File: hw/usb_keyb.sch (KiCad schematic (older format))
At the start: 103 parts, among them J1 POWER, J10 SPI, J11 ZX BUS, J12 ID, J13 ID, J2 Micro_SD_Card, J3 USB_1, J4 USB_2, J5 MX_ROW, J6 MX_COL, J7 I2C, J8 UART, J9 PROG, SW1 RESET, U1 LM3671MF, U2 STM32F407VETx, U3 STMPS2141STR, U4 STMPS2141STR, U5 74ALVC164245, U6 74ALVC164245, U7 74ALVC164245, Y1 8MHz

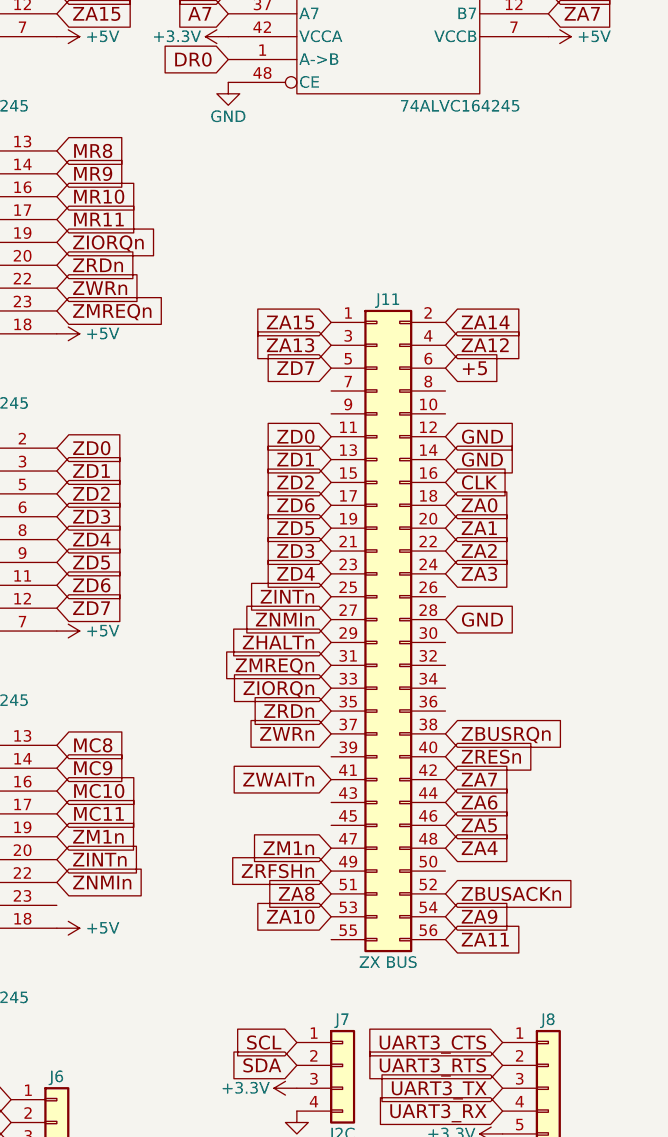
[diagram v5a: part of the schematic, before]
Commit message: Изменён разъём ZX-BUS, обновлена компоновка
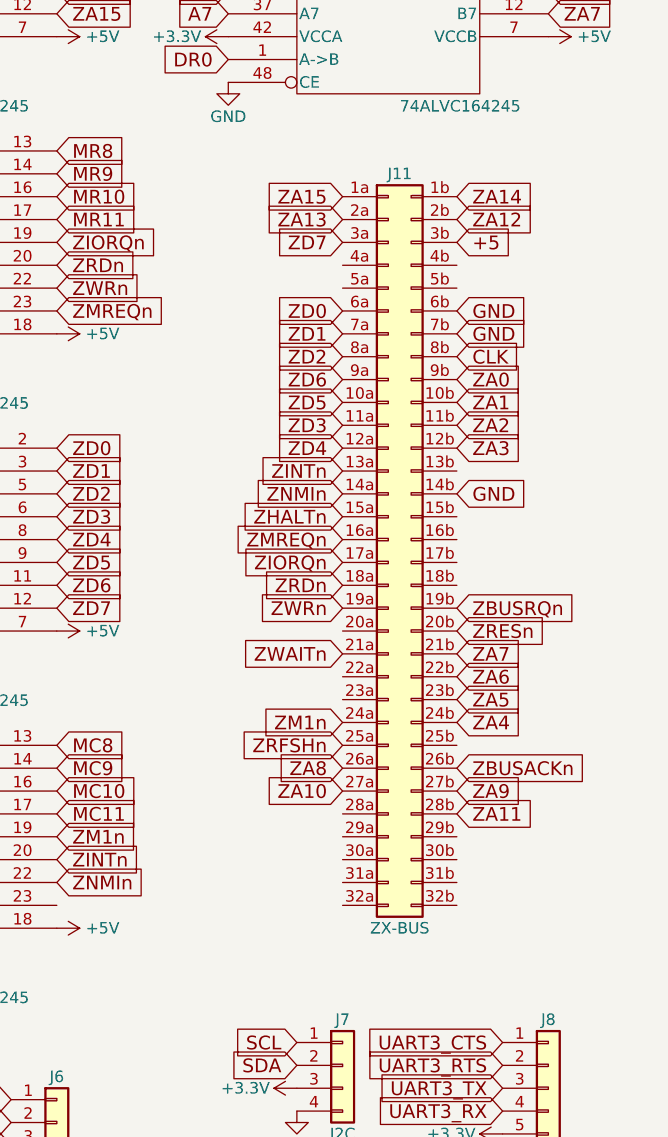
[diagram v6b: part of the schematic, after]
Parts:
- removed J11: ZX BUS, symbol Conn_02x28_Odd_Even
- added J11: ZX-BUS, Connectors_IEC_DIN:Socket_DIN41612-CaseC1-AC-Female-64Pin-2rows, symbol Conn_02x32_Row_Letter_Last
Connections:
- net +5: now also J11.3b (Pin_3b)
- net CLK: now also J11.8b (Pin_8b)
- net GND: now also J11.14b (Pin_14b), J11.6b (Pin_6b), J11.7b (Pin_7b)
- net ZA0: now also J11.9b (Pin_9b)
- net ZA1: now also J11.10b (Pin_10b)
- net ZA10: now also J11.27a (Pin_27a)
- net ZA11: now also J11.28b (Pin_28b)
- net ZA12: now also J11.2b (Pin_2b)
- net ZA13: now also J11.2a (Pin_2a)
- net ZA14: now also J11.1b (Pin_1b)
- net ZA15: now also J11.1a (Pin_1a)
- net ZA2: now also J11.11b (Pin_11b)
- net ZA3: now also J11.12b (Pin_12b)
- net ZA4: now also J11.24b (Pin_24b)
- net ZA5: now also J11.23b (Pin_23b)
- net ZA6: now also J11.22b (Pin_22b)
- net ZA7: now also J11.21b (Pin_21b)
- net ZA8: now also J11.26a (Pin_26a)
- net ZA9: now also J11.27b (Pin_27b)
- net ZBUSACKn: now also J11.26b (Pin_26b)
- net ZBUSRQn: now also J11.19b (Pin_19b)
- net ZD0: now also J11.6a (Pin_6a)
- net ZD1: now also J11.7a (Pin_7a)
- net ZD2: now also J11.8a (Pin_8a)
- net ZD3: now also J11.11a (Pin_11a)
- net ZD4: now also J11.12a (Pin_12a)
- net ZD5: now also J11.10a (Pin_10a)
- net ZD6: now also J11.9a (Pin_9a)
- net ZD7: now also J11.3a (Pin_3a)
- net ZHALTn: now also J11.15a (Pin_15a)
- net ZINTn: now also J11.13a (Pin_13a)
- net ZIORQn: now also J11.17a (Pin_17a)
- net ZM1n: now also J11.24a (Pin_24a)
- net ZMREQn: now also J11.16a (Pin_16a)
- net ZNMIn: now also J11.14a (Pin_14a)
- net ZRDn: now also J11.18a (Pin_18a)
- net ZRESn: now also J11.20b (Pin_20b)
- net ZRFSHn: now also J11.25a (Pin_25a)
- net ZWAITn: now also J11.21a (Pin_21a)
- net ZWRn: now also J11.19a (Pin_19a)
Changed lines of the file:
@@
 Text GLabel 10750 6550 2    60   Input ~ 0
 HS_ID
-Text GLabel 14450 5150 0    60   Input ~ 0
+Text GLabel 14500 4600 0    60   Input ~ 0
 ZA15
-Text GLabel 14950 5150 2    60   Input ~ 0
+Text GLabel 15000 4600 2    60   Input ~ 0
 ZA14
-Text GLabel 14450 5250 0    60   Input ~ 0
+Text GLabel 14500 4700 0    60   Input ~ 0
 ZA13
-Text GLabel 14950 5250 2    60   Input ~ 0
+Text GLabel 15000 4700 2    60   Input ~ 0
 ZA12
-Text GLabel 14450 5350 0    60   Input ~ 0
+Text GLabel 14500 4800 0    60   Input ~ 0
 ZD7
-Text GLabel 14950 5350 2    60   Input ~ 0
+Text GLabel 15000 4800 2    60   Input ~ 0
 +5
-Text GLabel 14450 5650 0    60   Input ~ 0
+Text GLabel 14500 5100 0    60   Input ~ 0
 ZD0
-Text GLabel 14450 5750 0    60   Input ~ 0
+Text GLabel 14500 5200 0    60   Input ~ 0
 ZD1
-Text GLabel 14450 5850 0    60   Input ~ 0
+Text GLabel 14500 5300 0    60   Input ~ 0
 ZD2
-Text GLabel 14450 5950 0    60   Input ~ 0
+Text GLabel 14500 5400 0    60   Input ~ 0
 ZD6
-Text GLabel 14450 6050 0    60   Input ~ 0
+Text GLabel 14500 5500 0    60   Input ~ 0
 ZD5
-Text GLabel 14450 6150 0    60   Input ~ 0
+Text GLabel 14500 5600 0    60   Input ~ 0
 ZD3
-Text GLabel 14450 6250 0    60   Input ~ 0
+Text GLabel 14500 5700 0    60   Input ~ 0
 ZD4
-Text GLabel 14450 6350 0    60   Input ~ 0
+Text GLabel 14500 5800 0    60   Input ~ 0
 ZINTn
-Text GLabel 14450 6450 0    60   Input ~ 0
+Text GLabel 14500 5900 0    60   Input ~ 0
 ZNMIn
-Text GLabel 14450 6550 0    60   Input ~ 0
+Text GLabel 14500 6000 0    60   Input ~ 0
 ZHALTn
-Text GLabel 14450 6650 0    60   Input ~ 0
+Text GLabel 14500 6100 0    60   Input ~ 0
 ZMREQn
-Text GLabel 14450 6750 0    60   Input ~ 0
+Text GLabel 14500 6200 0    60   Input ~ 0
 ZIORQn
-Text GLabel 14450 6850 0    60   Input ~ 0
+Text GLabel 14500 6300 0    60   Input ~ 0
 ZRDn
-Text GLabel 14450 6950 0    60   Input ~ 0
+Text GLabel 14500 6400 0    60   Input ~ 0
 ZWRn
-Text GLabel 14450 7150 0    60   Input ~ 0
+Text GLabel 14500 6600 0    60   Input ~ 0
 ZWAITn
-Text GLabel 14450 7450 0    60   Input ~ 0
+Text GLabel 14500 6900 0    60   Input ~ 0
 ZM1n
-Text GLabel 14450 7550 0    60   Input ~ 0
+Text GLabel 14500 7000 0    60   Input ~ 0
 ZRFSHn
-Text GLabel 14450 7650 0    60   Input ~ 0
+Text GLabel 14500 7100 0    60   Input ~ 0
 ZA8
-Text GLabel 14450 7750 0    60   Input ~ 0
+Text GLabel 14500 7200 0    60   Input ~ 0
 ZA10
-Text GLabel 14950 5650 2    60   Input ~ 0
+Text GLabel 15000 5100 2    60   Input ~ 0
 GND
-Text GLabel 14950 5750 2    60   Input ~ 0
+Text GLabel 15000 5200 2    60   Input ~ 0
 GND
-Text GLabel 14950 5850 2    60   Input ~ 0
+Text GLabel 15000 5300 2    60   Input ~ 0
 CLK
-Text GLabel 14950 5950 2    60   Input ~ 0
+Text GLabel 15000 5400 2    60   Input ~ 0
 ZA0
-Text GLabel 14950 6050 2    60   Input ~ 0
+Text GLabel 15000 5500 2    60   Input ~ 0
 ZA1
-Text GLabel 14950 6150 2    60   Input ~ 0
+Text GLabel 15000 5600 2    60   Input ~ 0
 ZA2
-Text GLabel 14950 6250 2    60   Input ~ 0
+Text GLabel 15000 5700 2    60   Input ~ 0
 ZA3
-Text GLabel 14950 6450 2    60   Input ~ 0
+Text GLabel 15000 5900 2    60   Input ~ 0
 GND
-Text GLabel 14950 6950 2    60   Input ~ 0
+Text GLabel 15000 6400 2    60   Input ~ 0
 ZBUSRQn
-Text GLabel 14950 7050 2    60   Input ~ 0
+Text GLabel 15000 6500 2    60   Input ~ 0
 ZRESn
-Text GLabel 14950 7150 2    60   Input ~ 0
+Text GLabel 15000 6600 2    60   Input ~ 0
 ZA7
-Text GLabel 14950 7250 2    60   Input ~ 0
+Text GLabel 15000 6700 2    60   Input ~ 0
 ZA6
-Text GLabel 14950 7350 2    60   Input ~ 0
+Text GLabel 15000 6800 2    60   Input ~ 0
 ZA5
-Text GLabel 14950 7450 2    60   Input ~ 0
+Text GLabel 15000 6900 2    60   Input ~ 0
 ZA4
-Text GLabel 14950 7650 2    60   Input ~ 0
+Text GLabel 15000 7100 2    60   Input ~ 0
 ZBUSACKn
-Text GLabel 14950 7750 2    60   Input ~ 0
+Text GLabel 15000 7200 2    60   Input ~ 0
 ZA9
-Text GLabel 14950 7850 2    60   Input ~ 0
+Text GLabel 15000 7300 2    60   Input ~ 0
 ZA11
-$Comp
-L Conn_02x28_Odd_Even J11
-U 1 1 5AB3CEB4
-P 14650 6450
-F 0 "J11" H 14700 7850 50  0000 C CNN
-F 1 "ZX BUS" H 14700 4950 50  0000 C CNN
-F 2 "" H 14650 6450 50  0001 C CNN
-F 3 "" H 14650 6450 50  0001 C CNN
-	1    14650 6450
-	1    0    0    -1
-$EndComp
 Text GLabel 13250 5700 2    60   Input ~ 0
 ZD0
@@
 Wire Wire Line
 	7650 2400 7650 2150
+$Comp
+L Conn_02x32_Row_Letter_Last J11
+U 1 1 5ABDA855
+P 14700 6100
+F 0 "J11" H 14750 7700 50  0000 C CNN
+F 1 "ZX-BUS" H 14750 4400 50  0000 C CNN
+F 2 "Connectors_IEC_DIN:Socket_DIN41612-CaseC1-AC-Female-64Pin-2rows" H 14700 6100 50  0001 C CNN
+F 3 "" H 14700 6100 50  0001 C CNN
+	1    14700 6100
+	1    0    0    -1
+$EndComp
 $EndSCHEMATC

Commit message: Убраны буферные элементы, все внешние сигналы будут Open Drain
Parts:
- removed C19, C20, C21, C22, C23, C24, C25, C26, C27, C28, C29, C30: 100n, Capacitors_SMD:C_0805, symbol C
- removed U5, U6, U7: 74ALVC164245, Housings_SSOP:SSOP-48_7.5x15.9mm_Pitch0.635mm, symbol 74ALVC164245
- added R48, R49, R50, R51, R52, R53, R54, R55, R56, R57, R58: 10k, Resistors_SMD:R_0805, symbol R
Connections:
- net A0 is gone; now on net ZA0: U2.84 (PD3/FSMC_CLK/USART2_CTS)
- net A1 is gone; now on net ZA1: U2.85 (PD4/FSMC_NOE/USART2_RTS)
- net A2 is gone; now on net ZA2: U2.86 (PD5/FSMC_NWE/USART2_TX)
- net A3 is gone; now on net ZA3: U2.87 (PD6/FSMC_NWAIT/USART2_RX)
- net A4 is gone; now on net ZA4: U2.88 (PD7/FSMC_NCE2/FSMC_NE1/USART2_CK)
- net A5 is gone; now on net ZA5: U2.55 (PD8/FSMC_D13/FSMC_DA13/USART3_TX)
- net A6 is gone; now on net ZA6: U2.56 (PD9/DAC_EXTI9/FSMC_D14/FSMC_DA14/USART3_RX)
- net A7 is gone; now on net ZA7: U2.57 (PD10/FSMC_D15/FSMC_DA15/USART3_CK)
- net C0 is gone; now on net ZD0: R36.2
- net C1 is gone; now on net ZD1: R37.2
- net C10 is gone; now on net MC10: R46.2
- net C11 is gone; now on net MC11: R47.2
- net C2 is gone; now on net ZD2: R38.2
- net C3 is gone; now on net ZD3: R39.2
- net C4 is gone; now on net ZD4: R40.2
- net C5 is gone; now on net ZD5: R41.2
- net C6 is gone; now on net ZD6: R42.2
- net C7 is gone; now on net ZD7: R43.2
- net C8 is gone; now on net MC8: R44.2
- net C9 is gone; now on net MC9: R45.2
- net I0 is gone; now on net ZA8: U2.15 (ADC1_IN10/ADC2_IN10/ADC3_IN10/USB_OTG_HS_ULPI_STP/PC0)
- net I1 is gone; now on net ZA9: U2.16 (ADC1_IN11/ADC2_IN11/ADC3_IN11/ETH_MDC/PC1)
- net I10 is gone; now on net MR10: U2.60 (PD13/FSMC_A18/TIM4_CH2)
- net I11 is gone; now on net MR11: U2.61 (PD14/FSMC_D0/FSMC_DA0/TIM4_CH3)
- net I2 is gone; now on net ZA10: U2.17 (ADC1_IN12/ADC2_IN12/ADC3_IN12/ETH_TXD2/I2S2_ext_SD/SPI2_MISO/USB_OTG_HS_ULPI_DIR/PC2)
- net I3 is gone; now on net ZA11: U2.18 (ADC1_IN13/ADC2_IN13/ADC3_IN13/ETH_TX_CLK/I2S2_SD/SPI2_MOSI/USB_OTG_HS_ULPI_NXT/PC3)
- net I4 is gone; now on net ZA12: U2.33 (ADC1_IN14/ADC2_IN14/ETH_RXD0/PC4)
- net I5 is gone; now on net ZA13: U2.34 (ADC1_IN15/ADC2_IN15/ETH_RXD1/PC5)
- net I6 is gone; now on net ZA14: U2.63 (DCMI_D0/I2S2_MCK/SDIO_D6/TIM3_CH1/TIM8_CH1/USART6_TX/PC6)
- net I7 is gone; now on net ZA15: U2.64 (DCMI_D1/I2S3_MCK/SDIO_D7/TIM3_CH2/TIM8_CH2/USART6_RX/PC7)
- net I8 is gone; now on net MR8: U2.81 (PD0/CAN1_RX/FSMC_D2/FSMC_DA2)
- net I9 is gone; now on net MR9: U2.82 (PD1/CAN1_TX/FSMC_D3/FSMC_DA3)
- net INT0 is gone; now on net ZIORQn: R20.2, U2.23 (ADC1_IN0/ADC2_IN0/ADC3_IN0/ETH_CRS/SYS_WKUP/TIM2_CH1/TIM2_ETR/TIM5_CH1/TIM8_ETR/UART4_TX/USART2_CTS/PA0)
- net INT1 is gone; now on net ZRDn: R21.2, U2.24 (ADC1_IN1/ADC2_IN1/ADC3_IN1/ETH_REF_CLK/ETH_RX_CLK/TIM2_CH2/TIM5_CH2/UART4_RX/USART2_RTS/PA1)
- net INT2 is gone; now on net ZWRn: R22.2, U2.25 (ADC1_IN2/ADC2_IN2/ADC3_IN2/ETH_MDIO/TIM2_CH3/TIM5_CH3/TIM9_CH1/USART2_TX/PA2)
- net INT3 is gone; now on net ZMREQn: R23.2, U2.26 (ADC1_IN3/ADC2_IN3/ADC3_IN3/ETH_COL/TIM2_CH4/TIM5_CH4/TIM9_CH2/USART2_RX/USB_OTG_HS_ULPI_D0/PA3)
- net INTn is gone; now on net ZINTn: U2.44 (PE13/FSMC_D10/FSMC_DA10/TIM1_CH3)
- net M1n is gone; now on net ZM1n: U2.43 (PE12/FSMC_D9/FSMC_DA9/TIM1_CH3N)
- net NMIn is gone; now on net ZNMIn: U2.45 (PE14/FSMC_D11/FSMC_DA11/TIM1_CH4)
- net O0 is gone; now on net ZD0: U2.97 (PE0/DCMI_D2/FSMC_NBL0/TIM4_ETR)
- net O1 is gone; now on net ZD1: U2.98 (PE1/DCMI_D3/FSMC_NBL1)
- net O10 is gone; now on net MC10: U2.41 (PE10/FSMC_D7/FSMC_DA7/TIM1_CH2N)
- net O11 is gone; now on net MC11: U2.42 (PE11/ADC1_EXTI11/ADC2_EXTI11/ADC3_EXTI11/FSMC_D8/FSMC_DA8/TIM1_CH2)
- net O2 is gone; now on net ZD2: U2.1 (PE2/ETH_TXD3/FSMC_A23/SYS_TRACECLK)
- net O3 is gone; now on net ZD3: U2.2 (PE3/FSMC_A19/SYS_TRACED0)
- net O4 is gone; now on net ZD4: U2.3 (PE4/DCMI_D4/FSMC_A20/SYS_TRACED1)
- net O5 is gone; now on net ZD5: U2.4 (PE5/DCMI_D6/FSMC_A21/SYS_TRACED2/TIM9_CH1)
- net O6 is gone; now on net ZD6: U2.5 (PE6/DCMI_D7/FSMC_A22/SYS_TRACED3/TIM9_CH2)
- net O7 is gone; now on net ZD7: U2.38 (PE7/FSMC_D4/FSMC_DA4/TIM1_ETR)
- net O8 is gone; now on net MC8: U2.39 (PE8/FSMC_D5/FSMC_DA5/TIM1_CH1N)
- net O9 is gone; now on net MC9: U2.40 (PE9/DAC_EXTI9/FSMC_D6/FSMC_DA6/TIM1_CH1)
- net R0 is gone; now on net ZA8: R24.2
- net R1 is gone; now on net ZA9: R25.2
- net R10 is gone; now on net MR10: R34.2
- net R11 is gone; now on net MR11: R35.2
- net R2 is gone; now on net ZA10: R26.2
- net R3 is gone; now on net ZA11: R27.2
- net R4 is gone; now on net ZA12: R28.2
- net R5 is gone; now on net ZA13: R29.2
- net R6 is gone; now on net ZA14: R30.2
- net R7 is gone; now on net ZA15: R31.2
- net R8 is gone; now on net MR8: R32.2
- net R9 is gone; now on net MR9: R33.2
- net +3V3: now also R48.1, R49.1, R50.1, R51.1, R52.1, R53.1, R54.1, R55.1, R56.1, R57.1, R58.1
- net ZA0: now also R51.2
- net ZA1: now also R52.2
- net ZA2: now also R53.2
- net ZA3: now also R54.2
- net ZA4: now also R55.2
- net ZA5: now also R56.2
- net ZA6: now also R57.2
- net ZA7: now also R58.2
- net ZINTn: now also R49.2
- net ZM1n: now also R48.2
- net ZNMIn: now also R50.2
- net DR0: no longer names the net of U2.35 (ADC1_IN8/ADC2_IN8/ETH_RXD2/TIM1_CH2N/TIM3_CH3/TIM8_CH2N/USB_OTG_HS_ULPI_D1/PB0)
- net DR1: no longer names the net of U2.36 (ADC1_IN9/ADC2_IN9/ETH_RXD3/TIM1_CH3N/TIM3_CH4/TIM8_CH3N/USB_OTG_HS_ULPI_D2/PB1)
- net DR2: no longer names the net of U2.37 (BOOT1/PB2)
- net DR3: no longer names the net of U2.89 (I2S3_CK/SPI1_SCK/SPI3_SCK/SYS_JTDO-SWO/TIM2_CH2/PB3)
- net DR4: no longer names the net of U2.90 (I2S3_ext_SD/SPI1_MISO/SPI3_MISO/SYS_JTRST/TIM3_CH1/PB4)
- net DR5: no longer names the net of U2.91 (CAN2_RX/DCMI_D10/ETH_PPS_OUT/I2C1_SMBA/I2S3_SD/SPI1_MOSI/SPI3_MOSI/TIM3_CH2/USB_OTG_HS_ULPI_D7/PB5)
- net DR6: no longer names the net of U2.95 (CAN1_RX/DCMI_D6/ETH_TXD3/I2C1_SCL/SDIO_D4/TIM10_CH1/TIM4_CH3/PB8)
- net DR7: no longer names the net of U2.96 (CAN1_TX/DAC_EXTI9/DCMI_D7/I2C1_SDA/I2S2_WS/SDIO_D5/SPI2_NSS/TIM11_CH1/TIM4_CH4/PB9)
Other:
- moved on the sheet: R20, R21, R22, R23

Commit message: Множественные изменения в схеме:
1) Заменён разъём USB на сдвоенный;
2) Добавлен Ethernet-PHY;
3) Изменено назначение служебных сигналов USB и интерфейсов;
4) внешние шины временно отключены от МК.
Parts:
- removed J12, J13: ID, Socket_Strips:Socket_Strip_Straight_1x01_Pitch2.54mm, symbol TEST_1P
- removed J4: USB_2, Connectors:USB_A, symbol USB_A
- added C19, C20, C21, C22, C24, C25, C26, C27, C29, C30, C31: 100n, Capacitors_SMD:C_0805, symbol C
- added C23, C28: 10u, Capacitors_Tantalum_SMD:CP_Tantalum_Case-A_EIA-3216-18_Reflow, symbol CP
- added J14: RJ45-TRANSFO, Projects:rj45_wurth-7499211122a, symbol RJ45-TRANSFO-RESCUE-usb_keyb
- added L2: 2.2µH, Inductors_SMD:L_0805, symbol L
- added R59, R60, R62, R63: 2k, Resistors_SMD:R_0805, symbol R
- added R61: 10k, Resistors_SMD:R_0805, symbol R
- added R64: 4k7, Resistors_SMD:R_0805, symbol R
- added R65: 150, Resistors_SMD:R_0805, symbol R
- added R66: 18, Resistors_SMD:R_0805, symbol R
- added R67, R68, R69, R70: 51, Resistors_SMD:R_0805, symbol R
- added R71, R72: 330, Resistors_SMD:R_0805, symbol R
- added U5: DP83848C, Housings_QFP:LQFP-48_7x7mm_Pitch0.5mm, symbol DP83848C
- added Y2: 50MHz, Crystals:Crystal_SMD_7050-4pin_7.0x5.0mm, symbol Crystal_GND24
- C17, C18: footprint Capacitors_Tantalum_SMD:CP_Tantalum_Case-A_EIA-3216-18_Hand -> Capacitors_Tantalum_SMD:CP_Tantalum_Case-A_EIA-3216-18_Reflow
- J2: symbol Micro_SD_Card -> Micro_SD_Card-RESCUE-usb_keyb
- J3: footprint Connectors:USB_A -> w_conn_pc:conn_usb_Ax2; symbol USB_A -> USB_A-RESCUE-usb_keyb
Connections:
- net +3V3: now also C19.1, C20.1, C21.1, C22.1, C23.1, C30.1, C31.1, J14.1 (TCT), J14.11 (LEDY_A), J14.13 (LEDG_A), L2.1, R59.1, R60.1, R61.1, R62.2, R63.2, R69.1, R70.1, U5.32 (IOVDD33), U5.48 (IOVDD33), Y2.4
- net CD: now also U2.64 (DCMI_D1/I2S3_MCK/SDIO_D7/TIM3_CH2/TIM8_CH2/USART6_RX/PC7); no longer U2.7 (ANTI_TAMP/RTC_AF1/PC13)
- net FS_PWR: now also U2.67 (I2C3_SCL/RCC_MCO_1/TIM1_CH1/USART1_CK/USB_OTG_FS_SOF/PA8); no longer U2.8 (RCC_OSC32_IN/PC14)
- net GND: now also J3.8 (GND), J3.9 (Shield), C19.2, C20.2, C21.2, C22.2, C23.2, C24.2, C25.2, C26.2, C27.2, C28.2, C29.2, C30.2, C31.2, J14.10, J14.15 (SHIELD), R66.1, U5.15 (AGND), U5.19 (AGND), U5.35 (IOGND), U5.36 (DGND), U5.47 (IOGND), Y2.2; no longer J3.5 (Shield)
- net HS_PWR: now also U2.63 (DCMI_D0/I2S2_MCK/SDIO_D6/TIM3_CH1/TIM8_CH1/USART6_TX/PC6); no longer U2.9 (ADC1_EXTI15/ADC2_EXTI15/ADC3_EXTI15/RCC_OSC32_OUT/PC15)
- net MC10: no longer U2.41 (PE10/FSMC_D7/FSMC_DA7/TIM1_CH2N)
- net MC11: no longer U2.42 (PE11/ADC1_EXTI11/ADC2_EXTI11/ADC3_EXTI11/FSMC_D8/FSMC_DA8/TIM1_CH2)
- net MC8: no longer U2.39 (PE8/FSMC_D5/FSMC_DA5/TIM1_CH1N)
- net MC9: no longer U2.40 (PE9/DAC_EXTI9/FSMC_D6/FSMC_DA6/TIM1_CH1)
- net MR10: no longer U2.60 (PD13/FSMC_A18/TIM4_CH2)
- net MR11: no longer U2.61 (PD14/FSMC_D0/FSMC_DA0/TIM4_CH3)
- net MR8: no longer U2.81 (PD0/CAN1_RX/FSMC_D2/FSMC_DA2)
- net MR9: no longer U2.82 (PD1/CAN1_TX/FSMC_D3/FSMC_DA3)
- net PA8: no longer U2.67 (I2C3_SCL/RCC_MCO_1/TIM1_CH1/USART1_CK/USB_OTG_FS_SOF/PA8)
- net SCL: no longer U2.92 (CAN2_TX/DCMI_D5/I2C1_SCL/TIM4_CH1/USART1_TX/PB6)
- net SDA: no longer U2.93 (DCMI_VSYNC/FSMC_NL/I2C1_SDA/TIM4_CH2/USART1_RX/PB7)
- net SPI_MISO: no longer U2.31 (ADC1_IN6/ADC2_IN6/DCMI_PIXCK/SPI1_MISO/TIM13_CH1/TIM1_BKIN/TIM3_CH1/TIM8_BKIN/PA6)
- net SPI_MOSI: no longer U2.32 (ADC1_IN7/ADC2_IN7/ETH_CRS_DV/ETH_RX_DV/SPI1_MOSI/TIM14_CH1/TIM1_CH1N/TIM3_CH2/TIM8_CH1N/PA7)
- net SPI_SCK: no longer U2.30 (ADC1_IN5/ADC2_IN5/DAC_OUT2/SPI1_SCK/TIM2_CH1/TIM2_ETR/TIM8_CH1N/USB_OTG_HS_ULPI_CK/PA5)
- net ZA0: no longer U2.84 (PD3/FSMC_CLK/USART2_CTS)
- net ZA1: no longer U2.85 (PD4/FSMC_NOE/USART2_RTS)
- net ZA10: no longer U2.17 (ADC1_IN12/ADC2_IN12/ADC3_IN12/ETH_TXD2/I2S2_ext_SD/SPI2_MISO/USB_OTG_HS_ULPI_DIR/PC2)
- net ZA11: no longer U2.18 (ADC1_IN13/ADC2_IN13/ADC3_IN13/ETH_TX_CLK/I2S2_SD/SPI2_MOSI/USB_OTG_HS_ULPI_NXT/PC3)
- net ZA12: no longer U2.33 (ADC1_IN14/ADC2_IN14/ETH_RXD0/PC4)
- net ZA13: no longer U2.34 (ADC1_IN15/ADC2_IN15/ETH_RXD1/PC5)
- net ZA14: no longer U2.63 (DCMI_D0/I2S2_MCK/SDIO_D6/TIM3_CH1/TIM8_CH1/USART6_TX/PC6)
- net ZA15: no longer U2.64 (DCMI_D1/I2S3_MCK/SDIO_D7/TIM3_CH2/TIM8_CH2/USART6_RX/PC7)
- net ZA2: no longer U2.86 (PD5/FSMC_NWE/USART2_TX)
- net ZA3: no longer U2.87 (PD6/FSMC_NWAIT/USART2_RX)
- net ZA4: no longer U2.88 (PD7/FSMC_NCE2/FSMC_NE1/USART2_CK)
- net ZA5: no longer U2.55 (PD8/FSMC_D13/FSMC_DA13/USART3_TX)
- net ZA6: no longer U2.56 (PD9/DAC_EXTI9/FSMC_D14/FSMC_DA14/USART3_RX)
- net ZA7: no longer U2.57 (PD10/FSMC_D15/FSMC_DA15/USART3_CK)
- net ZA8: no longer U2.15 (ADC1_IN10/ADC2_IN10/ADC3_IN10/USB_OTG_HS_ULPI_STP/PC0)
- net ZA9: no longer U2.16 (ADC1_IN11/ADC2_IN11/ADC3_IN11/ETH_MDC/PC1)
- net ZD0: no longer U2.97 (PE0/DCMI_D2/FSMC_NBL0/TIM4_ETR)
- net ZD1: no longer U2.98 (PE1/DCMI_D3/FSMC_NBL1)
- net ZD2: no longer U2.1 (PE2/ETH_TXD3/FSMC_A23/SYS_TRACECLK)
- net ZD3: no longer U2.2 (PE3/FSMC_A19/SYS_TRACED0)
- net ZD4: no longer U2.3 (PE4/DCMI_D4/FSMC_A20/SYS_TRACED1)
- net ZD5: no longer U2.4 (PE5/DCMI_D6/FSMC_A21/SYS_TRACED2/TIM9_CH1)
- net ZD6: no longer U2.5 (PE6/DCMI_D7/FSMC_A22/SYS_TRACED3/TIM9_CH2)
- net ZD7: no longer U2.38 (PE7/FSMC_D4/FSMC_DA4/TIM1_ETR)
- net ZINTn: no longer U2.44 (PE13/FSMC_D10/FSMC_DA10/TIM1_CH3)
- net ZIORQn: no longer U2.23 (ADC1_IN0/ADC2_IN0/ADC3_IN0/ETH_CRS/SYS_WKUP/TIM2_CH1/TIM2_ETR/TIM5_CH1/TIM8_ETR/UART4_TX/USART2_CTS/PA0)
- net ZM1n: no longer U2.43 (PE12/FSMC_D9/FSMC_DA9/TIM1_CH3N)
- net ZMREQn: no longer U2.26 (ADC1_IN3/ADC2_IN3/ADC3_IN3/ETH_COL/TIM2_CH4/TIM5_CH4/TIM9_CH2/USART2_RX/USB_OTG_HS_ULPI_D0/PA3)
- net ZNMIn: no longer U2.45 (PE14/FSMC_D11/FSMC_DA11/TIM1_CH4)
- net ZRDn: no longer U2.24 (ADC1_IN1/ADC2_IN1/ADC3_IN1/ETH_REF_CLK/ETH_RX_CLK/TIM2_CH2/TIM5_CH2/UART4_RX/USART2_RTS/PA1)
- net ZWRn: no longer U2.25 (ADC1_IN2/ADC2_IN2/ADC3_IN2/ETH_MDIO/TIM2_CH3/TIM5_CH3/TIM9_CH1/USART2_TX/PA2)
- net at R17.2: now also J3.6 (D-)
- net at R16.2: now also J3.7 (D+)
- net FS_ID renamed RX
- net FS_VBUS: no longer names the net of C17.1, J3.1 (VBUS), U3.1 (OUT)
- net FS_VBUS: no longer U2.68 (DAC_EXTI9/DCMI_D0/I2C3_SMBA/TIM1_CH2/USART1_TX/USB_OTG_FS_VBUS/PA9)
- net HS_ID renamed TXD0
- net TXD0: now also U5.3 (TXD_0)
- net HS_VBUS: no longer names the net of C18.1, U4.1 (OUT)
- net HS_VBUS: now also J3.5 (VBUS); no longer U2.52 (CAN2_TX/ETH_TXD1/I2S2_CK/SPI2_SCK/TIM1_CH1N/USART3_CTS/USB_OTG_HS_ULPI_D6/USB_OTG_HS_VBUS/PB13)
- net UART3_CTS: no longer names the net of U2.58 (PD11/ADC1_EXTI11/ADC2_EXTI11/ADC3_EXTI11/FSMC_A16/FSMC_CLE/USART3_CTS)
- net UART3_CTS: no longer J8.1 (Pin_1)
- net UART3_RTS: no longer names the net of U2.59 (PD12/FSMC_A17/FSMC_ALE/TIM4_CH1/USART3_RTS)
- net UART3_RTS: no longer J8.2 (Pin_2)
- net UART3_RX renamed TX_EN
- net TX_EN: no longer J8.4 (Pin_4)
- net UART3_TX: no longer names the net of U2.47 (ETH_RX_ER/I2C2_SCL/I2S2_CK/SPI2_SCK/TIM2_CH3/USART3_TX/USB_OTG_HS_ULPI_D3/PB10)
- net UART3_TX: no longer J8.3 (Pin_3)
- new net: R62.1, U5.20 (RESERVED)
- new net: R63.1, U5.21 (RESERVED)
- new net: L2.2, U5.22 (AVDD33)
- new net: R64.1, U5.24 (RBIAS)
- new net: R61.2, U5.29 (~RESET~)
- new net: R59.2, U5.39 (RX_DV/MII_MODE)
- new net: J14.12 (LEDY_K), R72.2
- new net: J14.14 (LEDG_K), R71.2
- new net: C29.1, R67.1, R68.1
- new net: R64.2, R65.2
- new net: R65.1, R66.2
- new net CRS: R60.2, U2.32 (ADC1_IN7/ADC2_IN7/ETH_CRS_DV/ETH_RX_DV/SPI1_MOSI/TIM14_CH1/TIM1_CH1N/TIM3_CH2/TIM8_CH1N/PA7), U5.40 (CRS/CRS_DV/LED_CFG)
- new net ECK: U2.24 (ADC1_IN1/ADC2_IN1/ADC3_IN1/ETH_REF_CLK/ETH_RX_CLK/TIM2_CH2/TIM5_CH2/UART4_RX/USART2_RTS/PA1), U5.34 (X1), Y2.3
- new net LA: R71.1, U5.26 (AN_EN/LED_ACT/COL)
- new net LL: R72.1, U5.28 (AN0/LED_LINK)
- new net MDC: U2.16 (ADC1_IN11/ADC2_IN11/ADC3_IN11/ETH_MDC/PC1), U5.31 (MDC)
- new net MDIO: U2.25 (ADC1_IN2/ADC2_IN2/ADC3_IN2/ETH_MDIO/TIM2_CH3/TIM5_CH3/TIM9_CH1/USART2_TX/PA2), U5.30 (MDIO)
- new net PFB: C24.1, C25.1, C26.1, C27.1, C28.1, U5.18 (PFBIN1), U5.23 (PFBOUT), U5.37 (PFBIN2)
- new net RD+: J14.4 (RD+), R69.2, U5.14 (RD+)
- new net RD-: J14.7 (RD-), R70.2, U5.13 (RD-)
- new net RXD0: U2.33 (ADC1_IN14/ADC2_IN14/ETH_RXD0/PC4), U5.43 (RXD_0/PHY_AD1)
- new net RXD1: U2.34 (ADC1_IN15/ADC2_IN15/ETH_RXD1/PC5), U5.44 (RXD_1/PHY_AD2)
- new net TD+: J14.2 (TD+), R67.2, U5.17 (TD+)
- new net TD-: J14.3 (TD-), R68.2, U5.16 (TD-)
- new net TX: U2.68 (DAC_EXTI9/DCMI_D0/I2C3_SMBA/TIM1_CH2/USART1_TX/USB_OTG_FS_VBUS/PA9)
- new net TXD1: U2.52 (CAN2_TX/ETH_TXD1/I2S2_CK/SPI2_SCK/TIM1_CH1N/USART3_CTS/USB_OTG_HS_ULPI_D6/USB_OTG_HS_VBUS/PB13), U5.4 (TXD_1)
- new net UART_CTS: J8.1 (Pin_1)
- new net UART_RTS: J8.2 (Pin_2)
- new net UART_RX: J8.4 (Pin_4)
- new net UART_TX: J8.3 (Pin_3)
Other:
- moved on the sheet: C17, C18, J10, J11, J5, J6, J7, J8, J9, R10, R11, R12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
